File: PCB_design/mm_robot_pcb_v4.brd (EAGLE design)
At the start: 34 x 46 mm, 35 parts, among them U1 PIC32

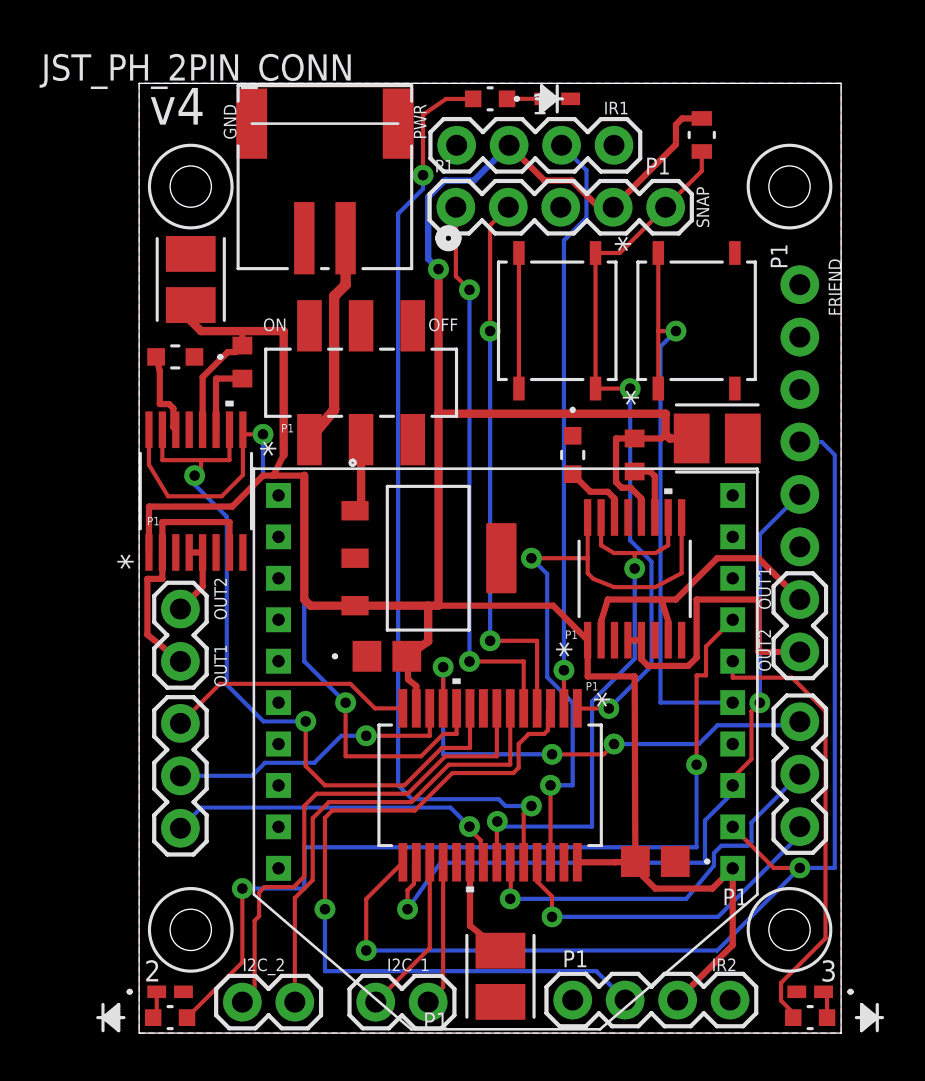
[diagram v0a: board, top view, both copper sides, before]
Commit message: Renamed PCB files so they're numbered correctly
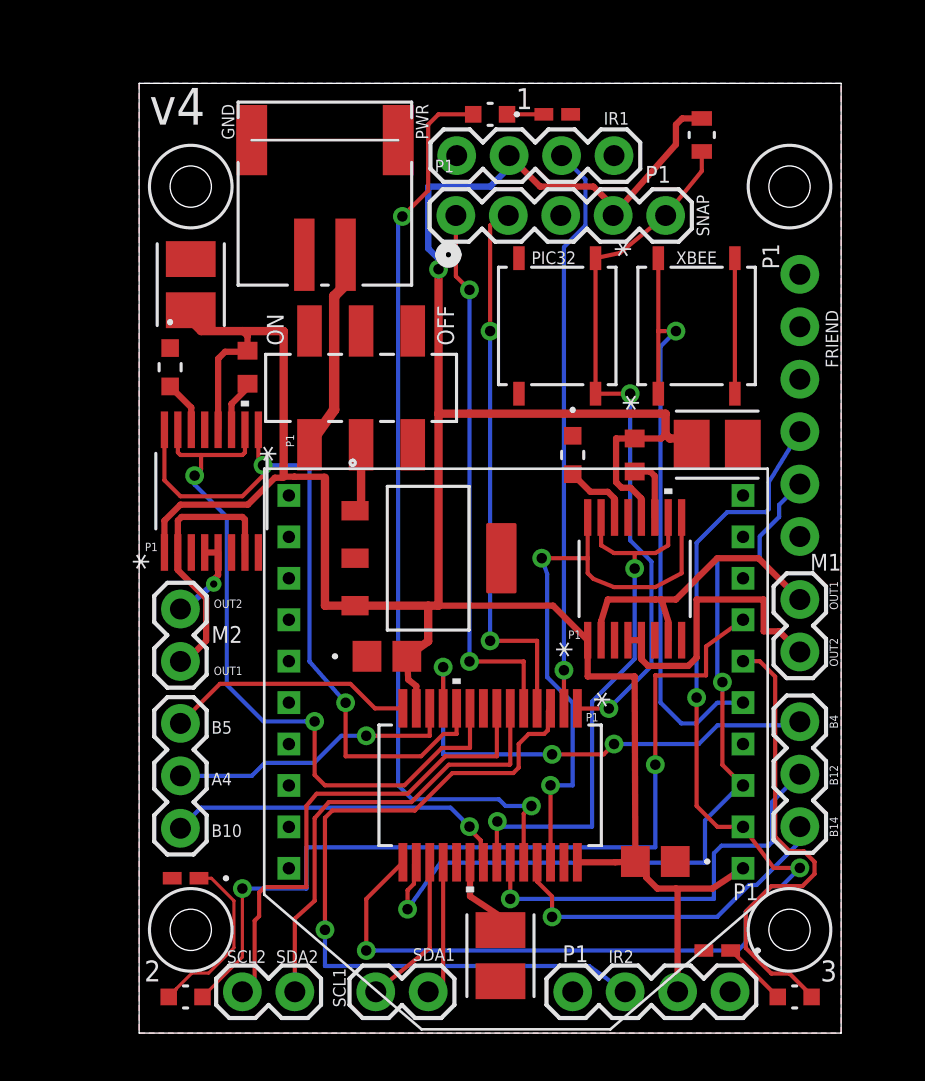
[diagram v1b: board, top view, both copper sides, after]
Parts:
- moved R7 5.55 mm to (2.25, 7.50), turned to 180 degrees
- moved R8 4.92 mm to (28.0, 4.00)
- moved LED2 1.25 mm to (2.25, 1.75)
- moved LED3 1.25 mm to (31.8, 1.75), turned to 0 degrees
- moved C10 1.00 mm to (17.5, 3.75)
- moved JST_PH_2PIN_CONN 0.80 mm to (10.0, 37.7)
- moved DRIVER2 0.75 mm to (3.50, 26.2)
- moved LED1 0.75 mm to (17.0, 44.5)
- moved R6 0.75 mm to (20.2, 44.5)
- moved C2_VINT2 0.56 mm to (1.50, 32.2), turned to 270 degrees
- moved FRIEND 0.50 mm to (32.0, 36.8)
- moved I2C_2 0.50 mm to (5.00, 2.00)
- moved IR1 0.50 mm to (23.0, 42.5)
- moved PCI-PINS4 0.50 mm to (14.0, 2.00)
- moved XBEE_ROBOT 0.50 mm to (18.2, 14.0)
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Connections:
- net RP12-AN12 renamed RB12-AN12
- removed net PB_C7: PIC_PB.3, PIC_PB.4
- net GND: now also PIC_PB.3, PIC_PB.4
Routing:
- net R7: track 1.32 -> 8.59 mm
- net PB_C7: track 6.57 -> 0.00 mm
- net GND: track 0.00 -> 6.57 mm
- net RPB7-PICTX-XBEERX: track 37.8 -> 40.5 mm
- net V+: track 142.9 -> 140.9 mm
- net R8: track 1.32 -> 3.22 mm
- net RPA3-OC3: track 36.2 -> 34.3 mm
- net VINT2: track 4.14 -> 2.52 mm
- net RB12-AN12: track 19.3 -> 20.7 mm
- net XBEE_RESET: track 29.2 -> 30.6 mm
- net VCP2: track 3.75 -> 2.55 mm
- net XBEE_PWM1: track 43.4 -> 42.4 mm
- net VCAP: track 4.98 -> 4.08 mm
- net RPB15-OC1: track 29.7 -> 28.9 mm
- net XBEE_PWM0: track 21.9 -> 22.7 mm
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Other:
- board text added: "A4"
- board text added: "B10"
- board text added: "B12"
- board text added: "B14"
- board text added: "B4"
- board text added: "B5"
- board text added: "M1"
- board text added: "M2"
- board text added: "PIC32"
- board text added: "SCL1"
- board text added: "SCL2 SDA2"
- board text added: "SDA1"
- board text added: "XBEE"
- board text removed: "I2C_1"
- board text removed: "I2C_2"
